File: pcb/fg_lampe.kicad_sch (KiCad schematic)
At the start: 37 parts, among them J1 ISP Port, J2 I^{2}C Debug, J3 RX/TX, J4 1792863, J5 1792863, J6 1792863, U1 ATmega328P-P, U2 L7805, U3 MAX1044, U4 MAX1044, U5 MCP4812, U8 MCP3008, Y1 16MHz

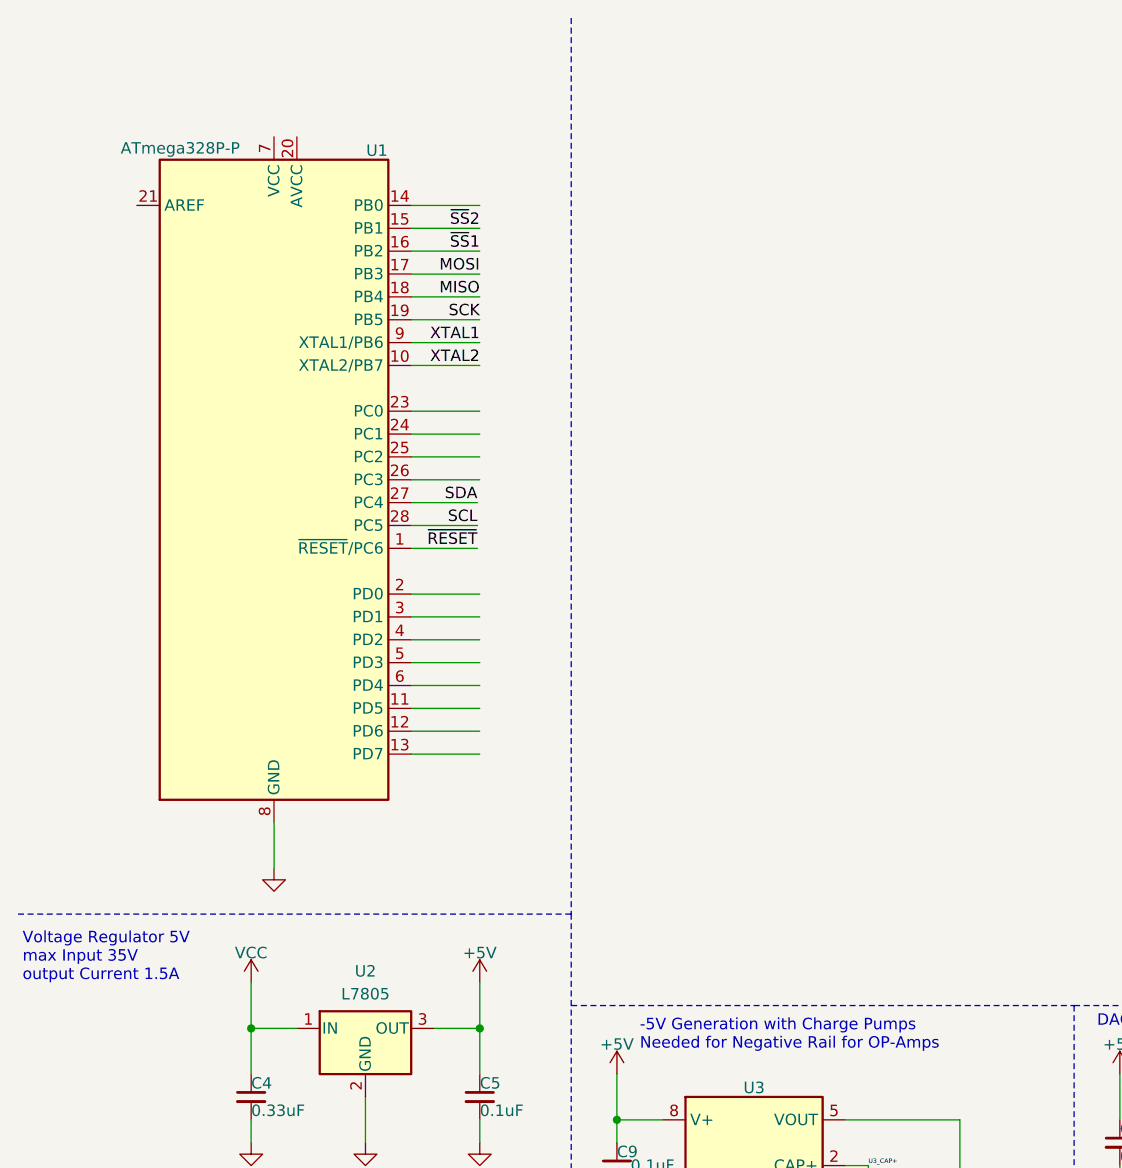
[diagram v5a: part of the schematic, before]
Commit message: reset button integrated
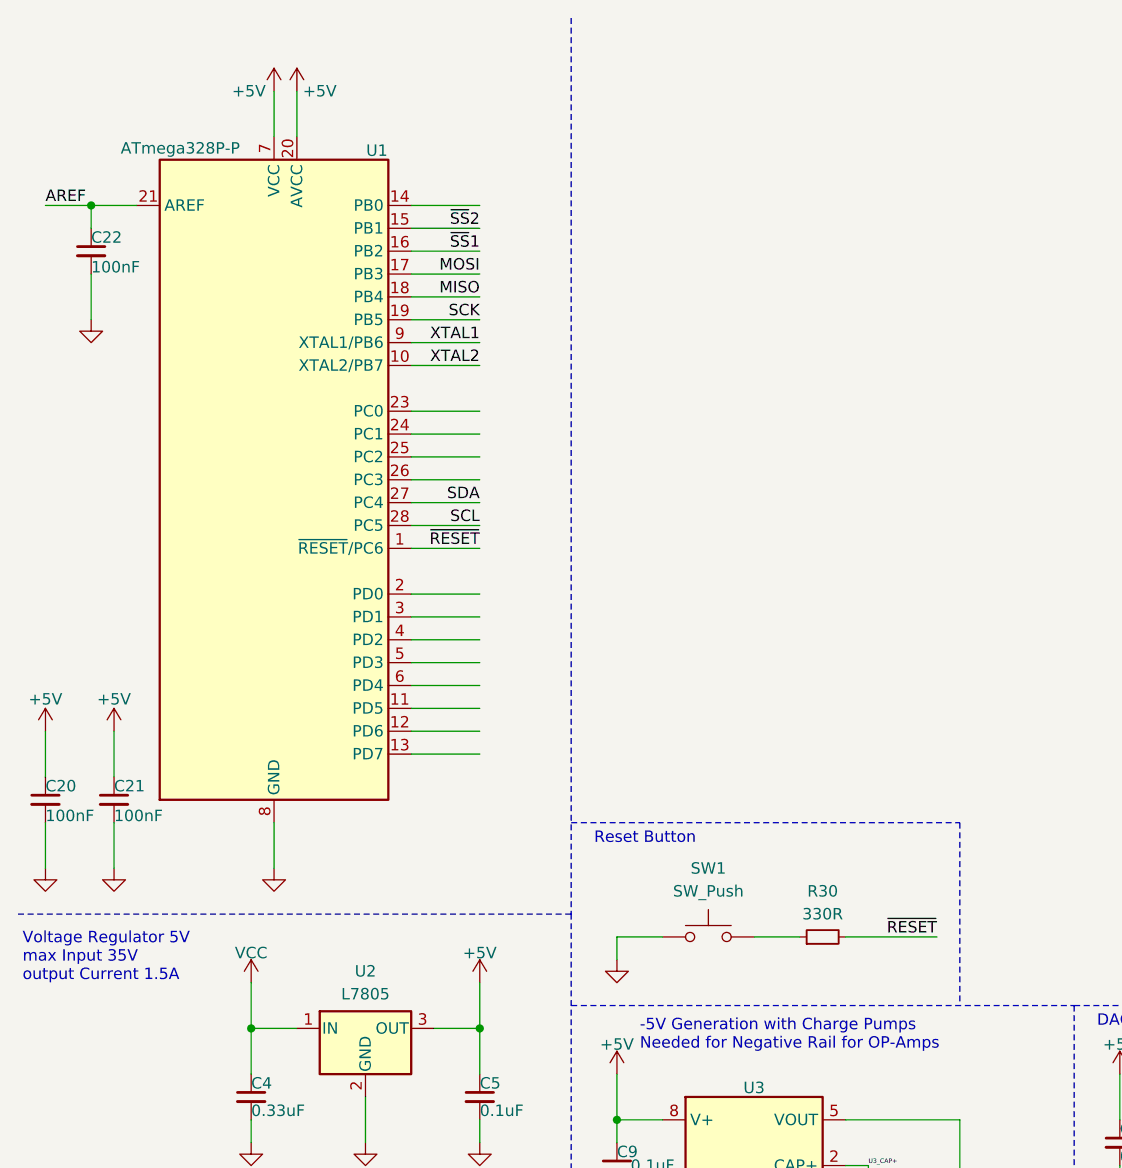
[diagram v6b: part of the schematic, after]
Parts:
- added C20, C21, C22: 100nF, Capacitor_THT:C_Disc_D3.8mm_W2.6mm_P2.50mm, symbol Device:C_Small
- added R30: 330R, symbol Device:R_Small
- added SW1: SW_Push, symbol Switch:SW_Push
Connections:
- net +5V: now also U1.20 (AVCC), U1.7 (VCC), C20.1, C21.1
- net GND: now also C20.2, C21.2, C22.2, SW1.1
- net ~{RESET}: now also R30.2
- net AREF: now reaches U1.21 (AREF)
- net AREF: now also C22.1
- new net: R30.1, SW1.2
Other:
- note added: "Reset Button"

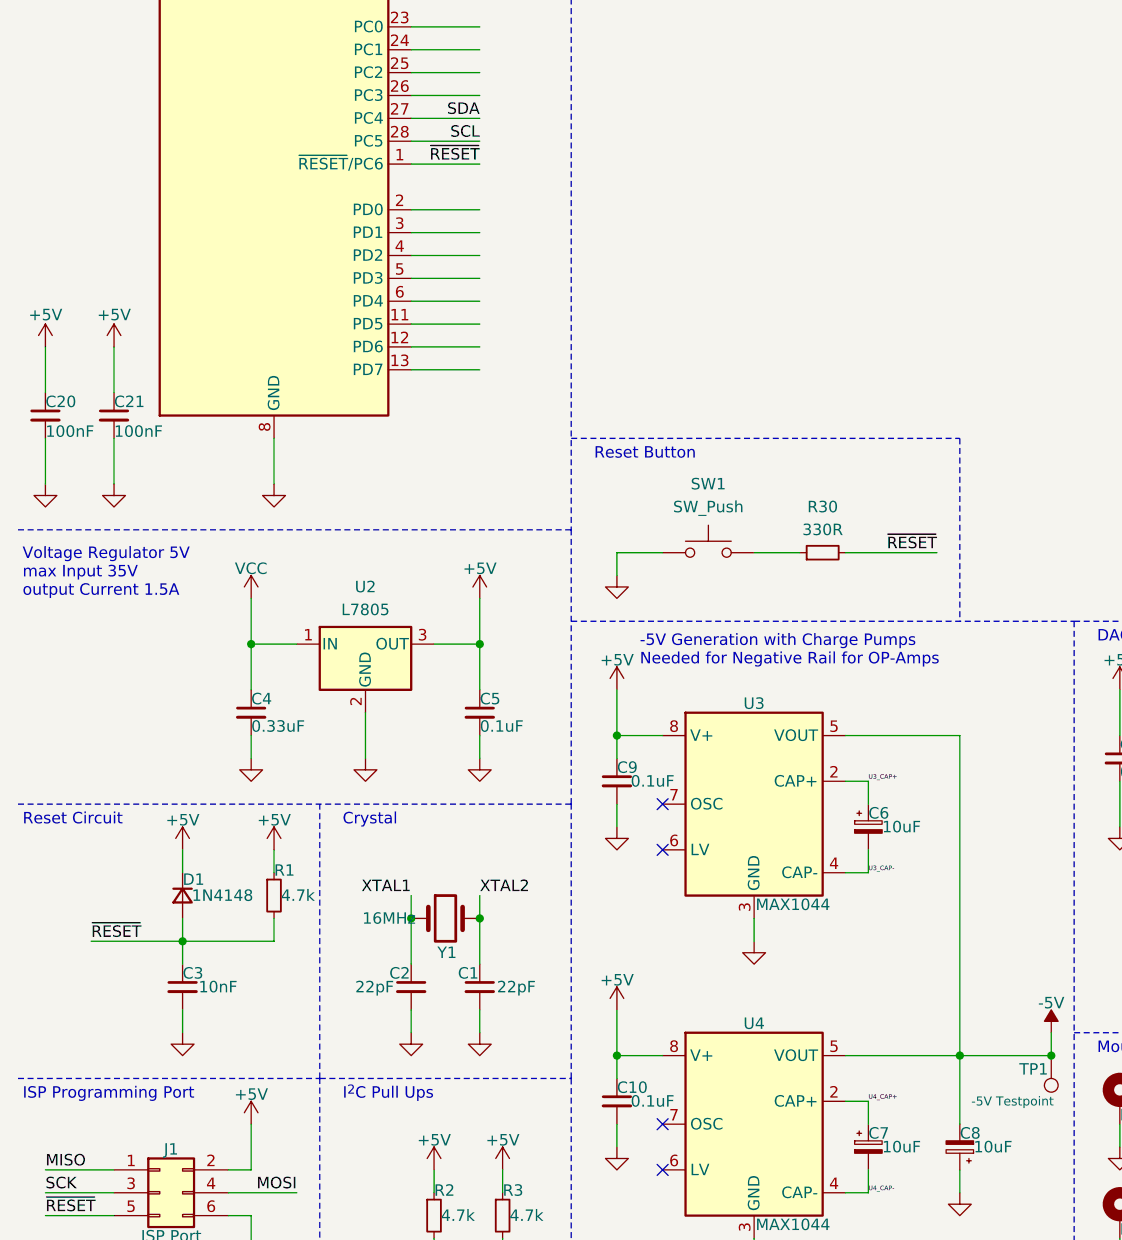
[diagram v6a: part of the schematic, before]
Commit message: buttons included
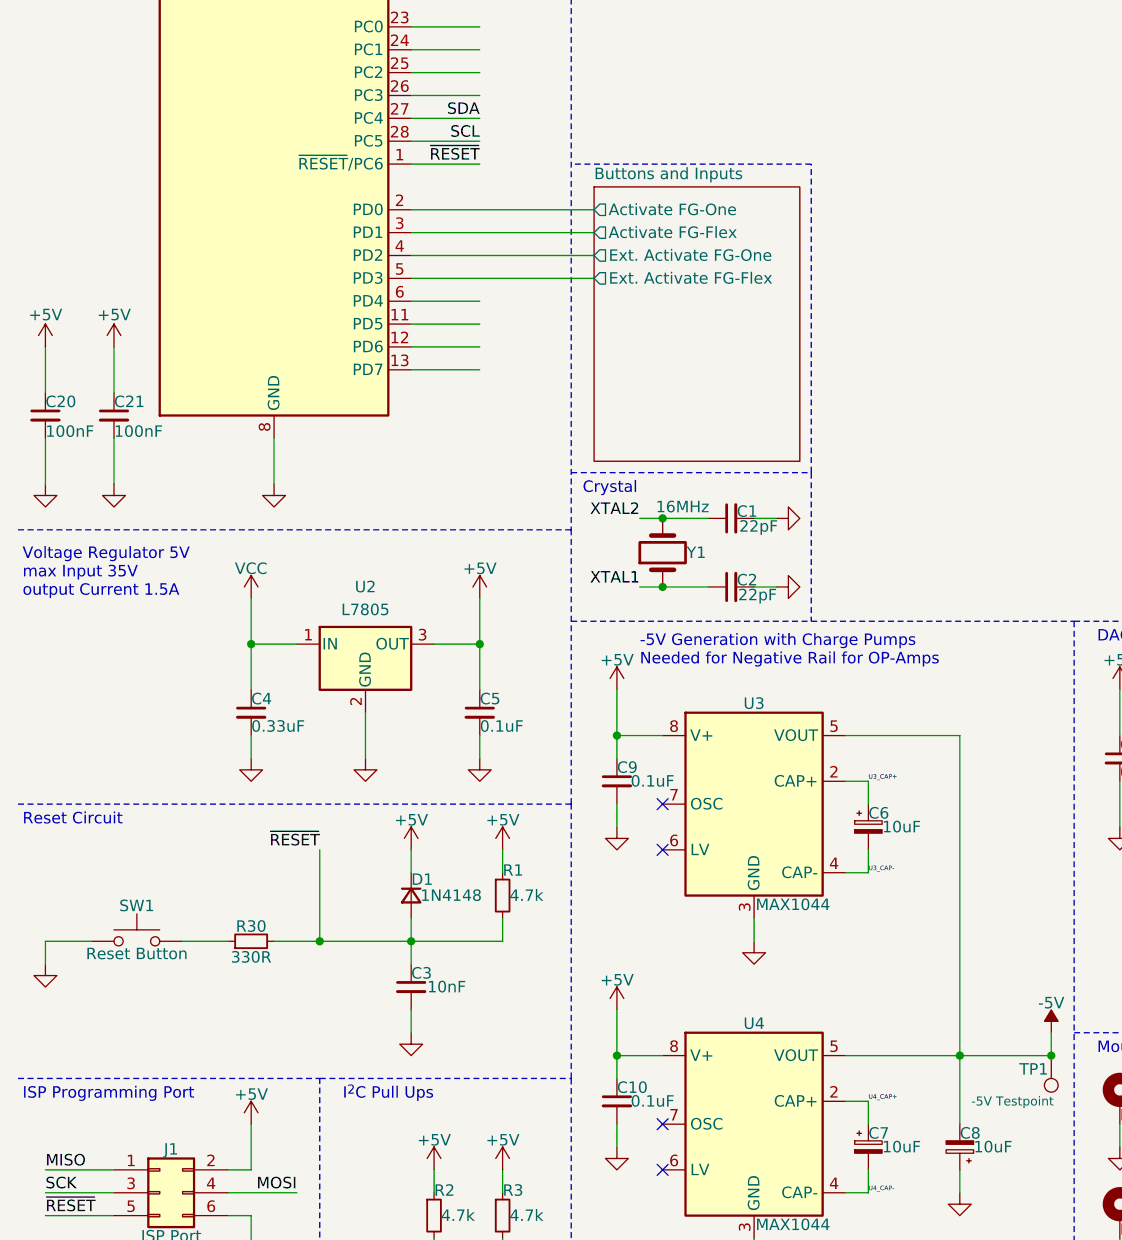
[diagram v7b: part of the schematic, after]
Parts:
- R30: footprint (none) -> Resistor_THT:R_Axial_DIN0207_L6.3mm_D2.5mm_P10.16mm_Horizontal; Part Nr. (none) -> CF14JT330R
- SW1: value SW_Push -> Reset Button; footprint (none) -> Button_Switch_THT:SW_PUSH_6mm_H5mm; Part Nr. (none) -> TS02-66-60-BK-160-SCR-D
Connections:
- net Buttons and Inputs/Activate FG-One: now reaches U1.2 (PD0)
- net Buttons and Inputs/Activate FG-Flex: now reaches U1.3 (PD1)
- net Buttons and Inputs/Ext. Activate FG-One: now reaches U1.4 (PD2)
- net Buttons and Inputs/Ext. Activate FG-Flex: now reaches U1.5 (PD3)
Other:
- added sheet Buttons and Inputs (buttons.kicad_sch)
- note removed: "Reset Button"
- moved on the sheet: C1, C2, C3, D1, R1, R30, SW1, Y1

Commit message: more stuff corrected
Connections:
- net activate fg_one: now reaches U1.12 (PD6)
- net activate fg_flex: now reaches U1.13 (PD7)
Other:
- note added: "Connection FG-Flex"
- note added: "Connection FG-One"
- note added: "Power Input"
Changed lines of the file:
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@@
   (no_connect (at 83.82 147.32))
   (no_connect (at 83.82 177.8))
-  (wire (pts (xy 55.88 91.44) (xy 63.5 91.44))
+  (wire (pts (xy 55.88 91.44) (xy 71.12 91.44))
     (stroke (width 0) (type default))
   )
@@
     (stroke (width 0) (type default))
   )
-  (wire (pts (xy 55.88 86.36) (xy 63.5 86.36))
+  (wire (pts (xy 55.88 86.36) (xy 71.12 86.36))
     (stroke (width 0) (type default))
   )
@@
     (stroke (width 0) (type default))
   )
-  (wire (pts (xy 55.88 38.1) (xy 63.5 38.1))
+  (wire (pts (xy 55.88 38.1) (xy 71.12 38.1))
     (stroke (width 0) (type default))
   )
@@
     (stroke (width 0) (type default))
   )
-  (wire (pts (xy 55.88 45.72) (xy 63.5 45.72))
+  (wire (pts (xy 55.88 45.72) (xy 71.12 45.72))
     (stroke (width 0) (type default))
   )
@@
     (stroke (width 0) (type default))
   )
-  (wire (pts (xy 55.88 63.5) (xy 63.5 63.5))
+  (wire (pts (xy 55.88 63.5) (xy 71.12 63.5))
     (stroke (width 0) (type default))
   )
@@
     (stroke (width 0) (type default))
   )
-  (wire (pts (xy 55.88 58.42) (xy 63.5 58.42))
-    (stroke (width 0) (type default))
-  )
   (wire (pts (xy 274.32 43.18) (xy 266.7 43.18))
     (stroke (width 0) (type default))
@@
     (stroke (width 0) (type default))
   )
-  (wire (pts (xy 55.88 93.98) (xy 63.5 93.98))
+  (wire (pts (xy 55.88 93.98) (xy 71.12 93.98))
     (stroke (width 0) (type default))
   )
@@
     (stroke (width 0) (type dash))
   )
-  (wire (pts (xy 55.88 68.58) (xy 63.5 68.58))
+  (wire (pts (xy 55.88 68.58) (xy 71.12 68.58))
     (stroke (width 0) (type default))
   )
@@
     (stroke (width 0) (type dash))
   )
+  (wire (pts (xy 55.88 58.42) (xy 71.12 58.42))
+    (stroke (width 0) (type default))
+  )
   (wire (pts (xy 274.32 101.6) (xy 281.94 101.6))
     (stroke (width 0) (type default))
   )
-  (wire (pts (xy 55.88 40.64) (xy 63.5 40.64))
+  (wire (pts (xy 55.88 40.64) (xy 71.12 40.64))
     (stroke (width 0) (type default))
   )
@@
     (stroke (width 0) (type default))
   )
-  (wire (pts (xy 55.88 60.96) (xy 63.5 60.96))
+  (wire (pts (xy 55.88 60.96) (xy 71.12 60.96))
+    (stroke (width 0) (type default))
+  )
+  (wire (pts (xy 55.88 33.02) (xy 71.12 33.02))
     (stroke (width 0) (type default))
   )
@@
     (stroke (width 0) (type default))
   )
-  (wire (pts (xy 55.88 35.56) (xy 63.5 35.56))
+  (wire (pts (xy 55.88 35.56) (xy 71.12 35.56))
     (stroke (width 0) (type default))
   )
@@
     (stroke (width 0) (type dash))
   )
+  (wire (pts (xy 200.66 132.08) (xy 215.9 132.08))
+    (stroke (width 0) (type default))
+  )
   (wire (pts (xy 15.24 101.6) (xy 15.24 106.68))
     (stroke (width 0) (type default))
@@
     (stroke (width 0) (type default))
   )
-  (wire (pts (xy 55.88 55.88) (xy 63.5 55.88))
-    (stroke (width 0) (type default))
-  )
   (polyline (pts (xy 220.98 12.192) (xy 220.98 68.58))
     (stroke (width 0) (type dash))
@@
     (stroke (width 0) (type default))
   )
-  (wire (pts (xy 55.88 50.8) (xy 63.5 50.8))
+  (wire (pts (xy 55.88 50.8) (xy 71.12 50.8))
     (stroke (width 0) (type default))
   )
@@
     (stroke (width 0) (type default))
   )
-  (wire (pts (xy 55.88 66.04) (xy 63.5 66.04))
+  (wire (pts (xy 55.88 66.04) (xy 71.12 66.04))
     (stroke (width 0) (type default))
   )
@@
     (stroke (width 0) (type default))
   )
-  (wire (pts (xy 55.88 71.12) (xy 63.5 71.12))
+  (wire (pts (xy 55.88 71.12) (xy 71.12 71.12))
     (stroke (width 0) (type default))
   )
@@
     (stroke (width 0) (type default))
   )
-  (wire (pts (xy 55.88 88.9) (xy 63.5 88.9))
+  (wire (pts (xy 55.88 88.9) (xy 71.12 88.9))
     (stroke (width 0) (type default))
   )
@@
     (stroke (width 0) (type default))
   )
-  (wire (pts (xy 55.88 48.26) (xy 63.5 48.26))
-    (stroke (width 0) (type default))
-  )
-  (wire (pts (xy 55.88 43.18) (xy 63.5 43.18))
+  (wire (pts (xy 55.88 48.26) (xy 71.12 48.26))
+    (stroke (width 0) (type default))
+  )
+  (wire (pts (xy 55.88 43.18) (xy 71.12 43.18))
     (stroke (width 0) (type default))
   )
@@
     (stroke (width 0) (type default))
   )
+  (wire (pts (xy 200.66 160.02) (xy 215.9 160.02))
+    (stroke (width 0) (type default))
+  )
   (wire (pts (xy 66.04 157.48) (xy 55.88 157.48))
     (stroke (width 0) (type default))
@@
     (stroke (width 0) (type default))
   )
+  (wire (pts (xy 55.88 55.88) (xy 71.12 55.88))
+    (stroke (width 0) (type default))
+  )
   (wire (pts (xy 83.82 110.49) (xy 88.9 110.49))
     (stroke (width 0) (type default))
@@
     (stroke (width 0) (type dash))
   )
-  (wire (pts (xy 55.88 33.02) (xy 63.5 33.02))
-    (stroke (width 0) (type default))
-  )
   (wire (pts (xy 38.1 124.46) (xy 38.1 129.54))
     (stroke (width 0) (type default))
@@
   )
   (text "Crystal" (at 74.93 107.95 0)
+    (effects (font (size 1.27 1.27)) (justify left bottom))
+  )
+  (text "Connection FG-Flex" (at 236.22 53.34 0)
     (effects (font (size 1.27 1.27)) (justify left bottom))
   )
@@
     (effects (font (size 1.27 1.27)) (justify left bottom))
   )
+  (text "Connection FG-One" (at 236.22 38.1 0)
+    (effects (font (size 1.27 1.27)) (justify left bottom))
+  )
   (text "-5V Generation with Charge Pumps\nNeeded for Negative Rail for OP-Amps"
     (at 81.28 127 0)
     (effects (font (size 1.27 1.27)) (justify left bottom))
   )
+  (text "Power Input" (at 236.22 22.86 0)
+    (effects (font (size 1.27 1.27)) (justify left bottom))
+  )
   (text "Current Sources to Controll the SMA Actuators" (at 200.66 124.46 0)
     (effects (font (size 1.27 1.27)) (justify left bottom))
@@
     (effects (font (size 1.27 1.27)) (justify left bottom))
   )
-  (label "~{SS}2" (at 63.5 35.56 180) (fields_autoplaced)
+  (label "~{SS}2" (at 71.12 35.56 180) (fields_autoplaced)
     (effects (font (size 1.27 1.27)) (justify right bottom))
   )
@@
     (effects (font (size 1.27 1.27)) (justify left bottom))
   )
-  (label "SDA" (at 63.5 66.04 180) (fields_autoplaced)
+  (label "SDA" (at 71.12 66.04 180) (fields_autoplaced)
     (effects (font (size 1.27 1.27)) (justify right bottom))
   )
@@
     (effects (font (size 1.27 1.27)) (justify right bottom))
   )
-  (label "~{SS}1" (at 63.5 38.1 180) (fields_autoplaced)
-    (effects (font (size 1.27 1.27)) (justify right bottom))
-  )
-  (label "XTAL2" (at 63.5 50.8 180) (fields_autoplaced)
-    (effects (font (size 1.27 1.27)) (justify right bottom))
-  )
-  (label "XTAL1" (at 63.5 48.26 180) (fields_autoplaced)
+  (label "activate fg_flex" (at 71.12 93.98 180) (fields_autoplaced)
+    (effects (font (size 1.27 1.27)) (justify right bottom))
+  )
+  (label "~{SS}1" (at 71.12 38.1 180) (fields_autoplaced)
+    (effects (font (size 1.27 1.27)) (justify right bottom))
+  )
+  (label "activate fg_one" (at 200.66 132.08 0) (fields_autoplaced)
+    (effects (font (size 1.27 1.27)) (justify left bottom))
+  )
+  (label "activate fg_flex" (at 200.66 160.02 0) (fields_autoplaced)
+    (effects (font (size 1.27 1.27)) (justify left bottom))
+  )
+  (label "XTAL2" (at 71.12 50.8 180) (fields_autoplaced)
+    (effects (font (size 1.27 1.27)) (justify right bottom))
+  )
+  (label "XTAL1" (at 71.12 48.26 180) (fields_autoplaced)
+    (effects (font (size 1.27 1.27)) (justify right bottom))
+  )
+  (label "activate fg_one" (at 71.12 91.44 180) (fields_autoplaced)
     (effects (font (size 1.27 1.27)) (justify right bottom))
   )
@@
     (effects (font (size 0.5 0.5)) (justify left bottom))
   )
-  (label "SCL" (at 63.5 68.58 180) (fields_autoplaced)
+  (label "SCL" (at 71.12 68.58 180) (fields_autoplaced)
     (effects (font (size 1.27 1.27)) (justify right bottom))
   )
@@
     (effects (font (size 1.27 1.27)) (justify left bottom))
   )
-  (label "MOSI" (at 63.5 40.64 180) (fields_autoplaced)
+  (label "MOSI" (at 71.12 40.64 180) (fields_autoplaced)
     (effects (font (size 1.27 1.27)) (justify right bottom))
   )
@@
     (effects (font (size 1.27 1.27)) (justify left bottom))
   )
-  (label "~{RESET}" (at 63.5 71.12 180) (fields_autoplaced)
-    (effects (font (size 1.27 1.27)) (justify right bottom))
-  )
-  (label "SCK" (at 63.5 45.72 180) (fields_autoplaced)
+  (label "~{RESET}" (at 71.12 71.12 180) (fields_autoplaced)
+    (effects (font (size 1.27 1.27)) (justify right bottom))
+  )
+  (label "SCK" (at 71.12 45.72 180) (fields_autoplaced)
     (effects (font (size 1.27 1.27)) (justify right bottom))
   )
@@
     (effects (font (size 0.5 0.5)) (justify left bottom))
   )
-  (label "MISO" (at 63.5 43.18 180) (fields_autoplaced)
-    (effects (font (size 1.27 1.27)) (justify right bottom))
-  )
+  (label "MISO" (at 71.12 43.18 180) (fields_autoplaced)
+    (effects (font (size 1.27 1.27)) (justify right bottom))
+  )
